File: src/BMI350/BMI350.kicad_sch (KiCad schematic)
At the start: 7 parts, among them U1 STM32H750VBTx, U2 BMM350

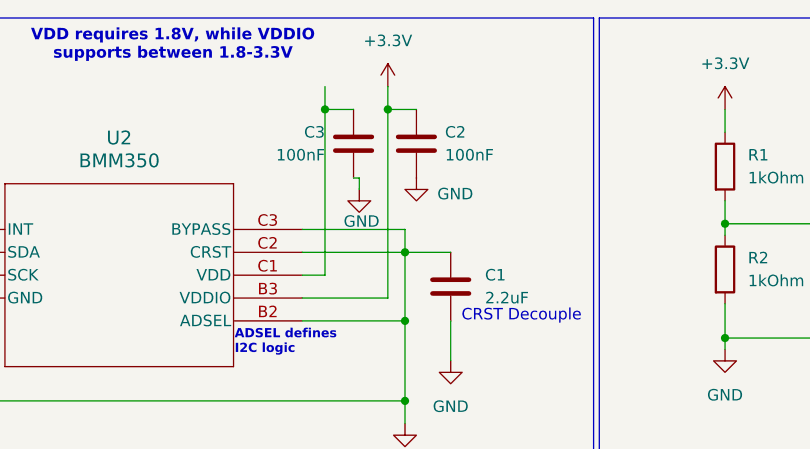
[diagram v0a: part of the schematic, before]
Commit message: BMM forgot
Forgot to save files before pushing
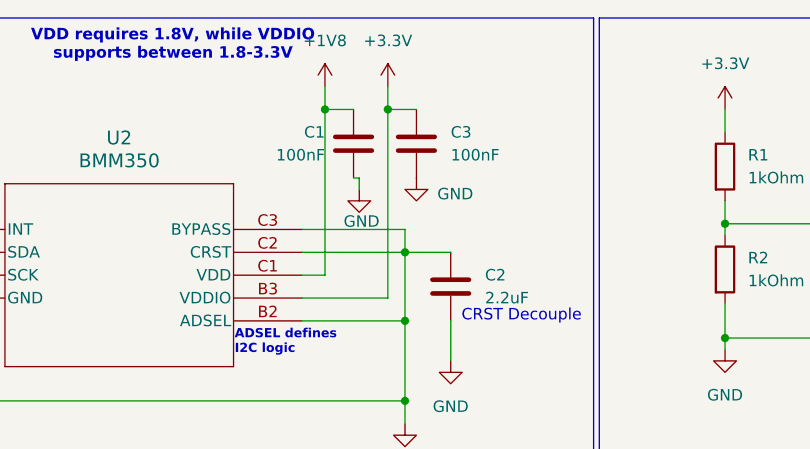
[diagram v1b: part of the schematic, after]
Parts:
- C1: renamed from C3; footprint Capacitor_SMD:C_0402_1005Metric -> Capacitor_SMD:C_0201_0603Metric
- C2: renamed from C1; footprint Capacitor_SMD:C_0402_1005Metric -> Capacitor_SMD:C_0201_0603Metric
- C3: renamed from C2; footprint Capacitor_SMD:C_0402_1005Metric -> Capacitor_SMD:C_0201_0603Metric
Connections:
- net +1V8: now also C1.2, U2.C1 (VDD)
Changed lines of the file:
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@@
 		(on_board yes)
 		(dnp no)
-		(property "Reference" "C3"
+		(property "Reference" "C1"
 			(at 156.21 26.6699 0)
 			(effects
@@
 			)
 		)
-		(property "Footprint" "Capacitor_SMD:C_0402_1005Metric"
+		(property "Footprint" "Capacitor_SMD:C_0201_0603Metric"
 			(at 160.3502 24.13 0)
 			(effects
@@
 			(project "BMI350"
 				(path "/5c9baf5e-0e0f-4389-833f-bb0eff9d07fc"
-					(reference "C3")
+					(reference "C1")
 					(unit 1)
 				)
@@
 	)
 	(symbol
+		(lib_id "power:+1V8")
+		(at 156.21 21.59 0)
+		(unit 1)
+		(exclude_from_sim no)
+		(in_bom yes)
+		(on_board yes)
+		(dnp no)
+		(fields_autoplaced yes)
+		(property "Reference" "#PWR03"
+			(at 156.21 25.4 0)
+			(effects
+				(font
+					(size 1.27 1.27)
+				)
+				(hide yes)
+			)
+		)
+		(property "Value" "+1V8"
+			(at 156.21 16.51 0)
+			(effects
+				(font
+					(size 1.27 1.27)
+				)
+			)
+		)
+		(property "Footprint" ""
+			(at 156.21 21.59 0)
+			(effects
+				(font
+					(size 1.27 1.27)
+				)
+				(hide yes)
+			)
+		)
+		(property "Datasheet" ""
+			(at 156.21 21.59 0)
+			(effects
+				(font
+					(size 1.27 1.27)
+				)
+				(hide yes)
+			)
+		)
+		(property "Description" "Power symbol creates a global label with name \"+1V8\""
+			(at 156.21 21.59 0)
+			(effects
+				(font
+					(size 1.27 1.27)
+				)
+				(hide yes)
+			)
+		)
+		(pin "1"
+		)
+		(instances
+			(project ""
+				(path "/5c9baf5e-0e0f-4389-833f-bb0eff9d07fc"
+					(reference "#PWR03")
+					(unit 1)
+				)
+			)
+		)
+	)
+	(symbol
 		(lib_id "Device:C")
 		(at 166.37 27.94 0)
@@
 		(dnp no)
 		(fields_autoplaced yes)
-		(property "Reference" "C2"
-			(at 169.545 26.6699 0)
+		(property "Reference" "C3"
+			(at 170.18 26.6699 0)
 			(effects
 				(font
@@
 		)
 		(property "Value" "100nF"
-			(at 169.545 29.2099 0)
+			(at 170.18 29.2099 0)
 			(effects
 				(font
@@
 			)
 		)
-		(property "Footprint" "Capacitor_SMD:C_0402_1005Metric"
+		(property "Footprint" "Capacitor_SMD:C_0201_0603Metric"
 			(at 167.3352 31.75 0)
 			(effects
@@
 			(project ""
 				(path "/5c9baf5e-0e0f-4389-833f-bb0eff9d07fc"
-					(reference "C2")
+					(reference "C3")
 					(unit 1)
 				)
@@
 		(dnp no)
 		(fields_autoplaced yes)
-		(property "Reference" "C1"
+		(property "Reference" "C2"
 			(at 173.99 42.5449 0)
 			(effects
@@
 			)
 		)
-		(property "Footprint" "Capacitor_SMD:C_0402_1005Metric"
+		(property "Footprint" "Capacitor_SMD:C_0201_0603Metric"
 			(at 171.1452 47.625 0)
 			(effects
@@
 			(project ""
 				(path "/5c9baf5e-0e0f-4389-833f-bb0eff9d07fc"
-					(reference "C1")
-					(unit 1)
-				)
+					(reference "C2")
+					(unit 1)
+				)

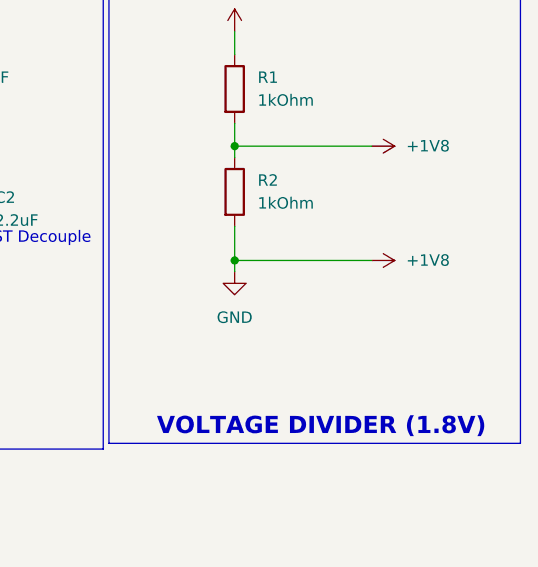
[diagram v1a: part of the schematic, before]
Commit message: Voltage Divider
Fixed voltage divider outputs
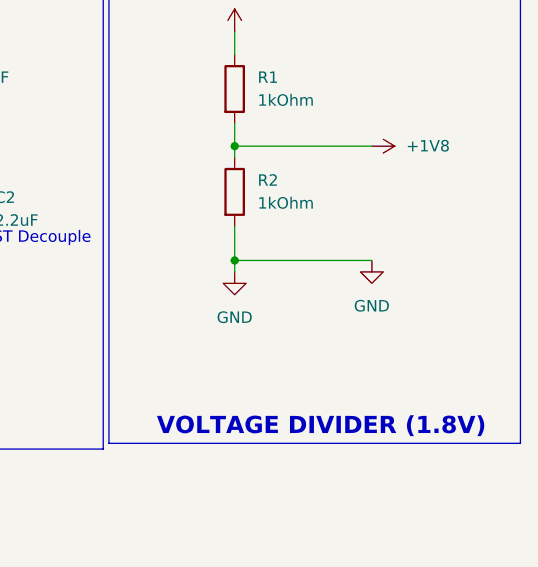
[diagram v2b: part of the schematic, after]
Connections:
- net +1V8: no longer C1.1, C2.1, C2.2, C3.2, R2.2, U2.B1 (GND), U2.B2 (ADSEL), U2.C2 (CRST), U2.C3 (BYPASS)
- new net GND: C1.1, C2.1, C2.2, C3.2, R2.2, U2.B1 (GND), U2.B2 (ADSEL), U2.C2 (CRST), U2.C3 (BYPASS)
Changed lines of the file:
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@@
-	)
-	(symbol
-		(lib_id "power:+1V8")
-		(at 215.9 49.53 270)
-		(unit 1)
-		(exclude_from_sim no)
-		(in_bom yes)
-		(on_board yes)
-		(dnp no)
-		(fields_autoplaced yes)
-		(property "Reference" "#PWR07"
-			(at 212.09 49.53 0)
-			(effects
-				(font
-					(size 1.27 1.27)
-				)
-				(hide yes)
-			)
-		)
-		(property "Value" "+1V8"
-			(at 219.71 49.5299 90)
-			(effects
-				(font
-					(size 1.27 1.27)
-				)
-				(justify left)
-			)
-		)
-		(property "Footprint" ""
-			(at 215.9 49.53 0)
-			(effects
-				(font
-					(size 1.27 1.27)
-				)
-				(hide yes)
-			)
-		)
-		(property "Datasheet" ""
-			(at 215.9 49.53 0)
-			(effects
-				(font
-					(size 1.27 1.27)
-				)
-				(hide yes)
-			)
-		)
-		(property "Description" "Power symbol creates a global label with name \"+1V8\""
-			(at 215.9 49.53 0)
-			(effects
-				(font
-					(size 1.27 1.27)
-				)
-				(hide yes)
-			)
-		)
-		(pin "1"
-		)
-		(instances
-			(project ""
-				(path "/5c9baf5e-0e0f-4389-833f-bb0eff9d07fc"
-					(reference "#PWR07")
-					(unit 1)
-				)
-			)
-		)
 	)
 	(symbol
@@
 					(unit 1)
 				)
+			)
+		)
+	)
+	(symbol
+		(lib_id "power:GND")
+		(at 215.9 49.53 0)
+		(unit 1)
+		(exclude_from_sim no)
+		(in_bom yes)
+		(on_board yes)
+		(dnp no)
+		(fields_autoplaced yes)
+		(property "Reference" "#PWR07"
+			(at 215.9 55.88 0)
+			(effects
+				(font
+					(size 1.27 1.27)
+				)
+				(hide yes)
+			)
+		)
+		(property "Value" "GND"
+			(at 215.9 54.61 0)
+			(effects
+				(font
+					(size 1.27 1.27)
+				)
+			)
+		)
+		(property "Footprint" ""
+			(at 215.9 49.53 0)
+			(effects
+				(font
+					(size 1.27 1.27)
+				)
+				(hide yes)
+			)
+		)
+		(property "Datasheet" ""
+			(at 215.9 49.53 0)
+			(effects
+				(font
+					(size 1.27 1.27)
+				)
+				(hide yes)
+			)
+		)
+		(property "Description" "Power symbol creates a global label with name \"GND\" , ground"
+			(at 215.9 49.53 0)
+			(effects
+				(font
+					(size 1.27 1.27)
+				)
+				(hide yes)
+			)
+		)
+		(pin "1"
+		)
+		(instances
+			(project ""
+				(path "/5c9baf5e-0e0f-4389-833f-bb0eff9d07fc"
+					(reference "#PWR07")
+					(unit 1)
+				)

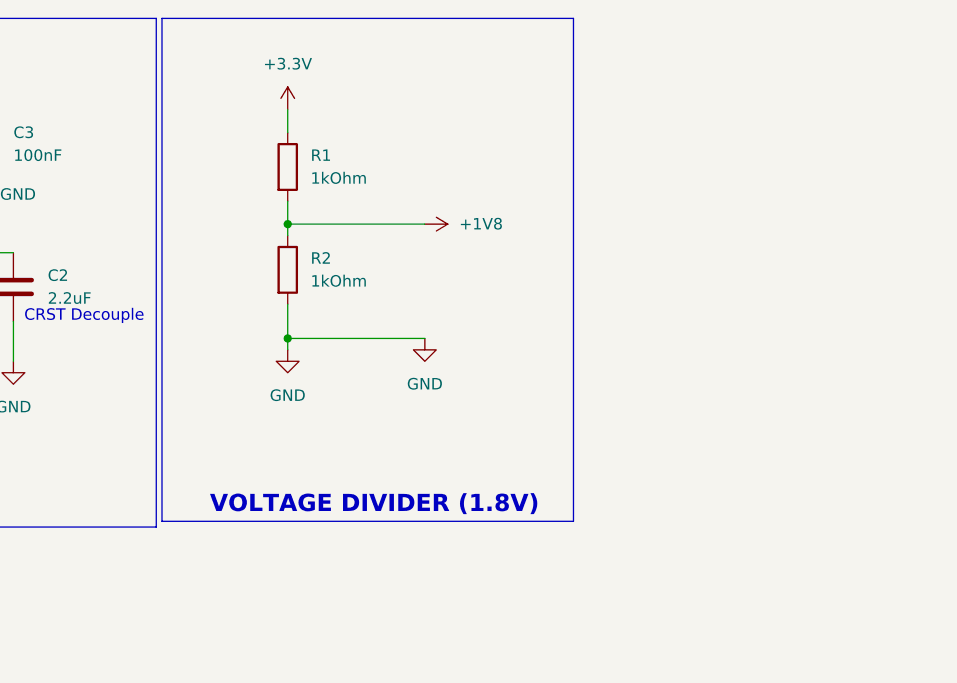
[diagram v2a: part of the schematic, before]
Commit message: Buck Converter
Redid BM350 breakout schematic with 3.3-1.8 buck converter instead of voltage divider
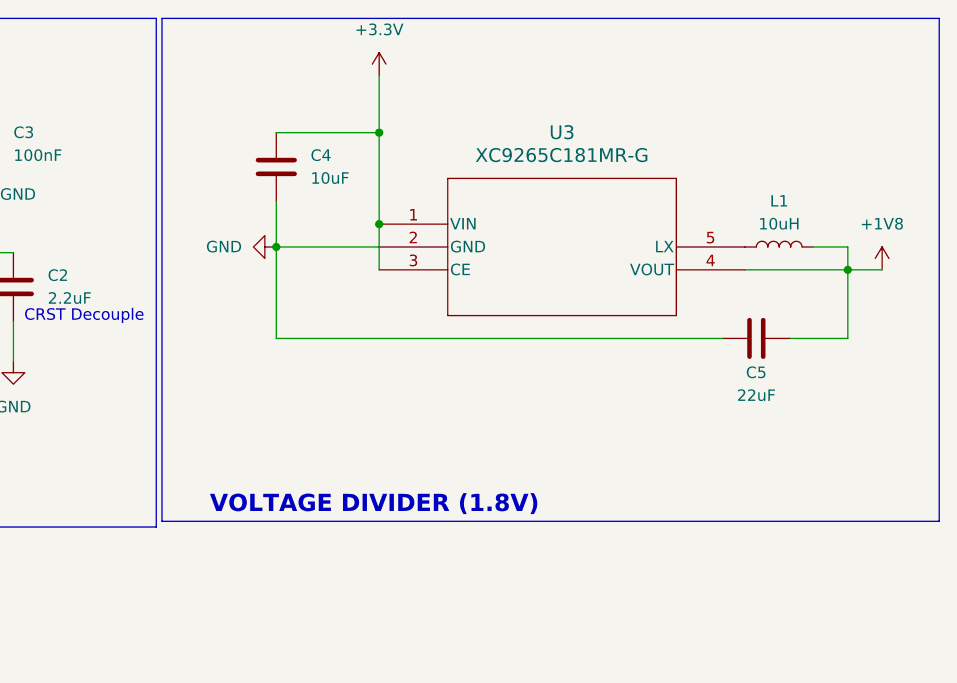
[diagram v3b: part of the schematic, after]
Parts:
- removed R1, R2: 1kOhm, Resistor_SMD:R_0201_0603Metric, symbol Device:R
- added C4: 10uF, Capacitor_SMD:C_0201_0603Metric, symbol Device:C
- added C5: 22uF, Capacitor_SMD:C_0201_0603Metric, symbol Device:C
- added L1: 10uH, Inductor_SMD:L_0201_0603Metric, symbol Device:L
- added U3: XC9265C181MR-G, XC9529:SOT_181MR-G_TOR, symbol XC9265:XC9265C181MR-G
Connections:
- net +1V8: now also C5.2, L1.2, U3.4 (VOUT)
- net +3.3V: now also C4.1, U3.1 (VIN), U3.3 (CE)
- net GND: now also C4.2, C5.1, U3.2 (GND)
- new net: L1.1, U3.5 (LX)

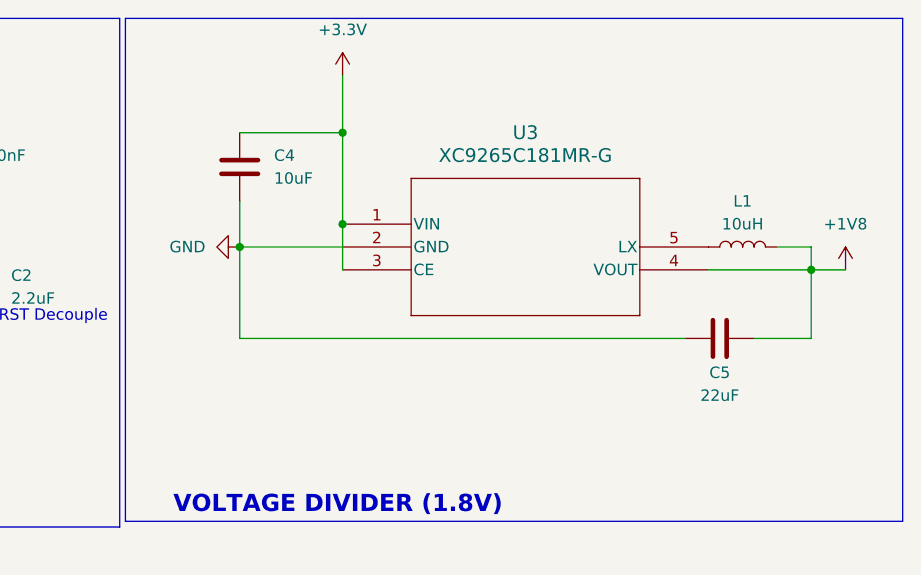
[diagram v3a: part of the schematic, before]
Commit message: S-85S1A
Added S-85S1A to flight computer schematic
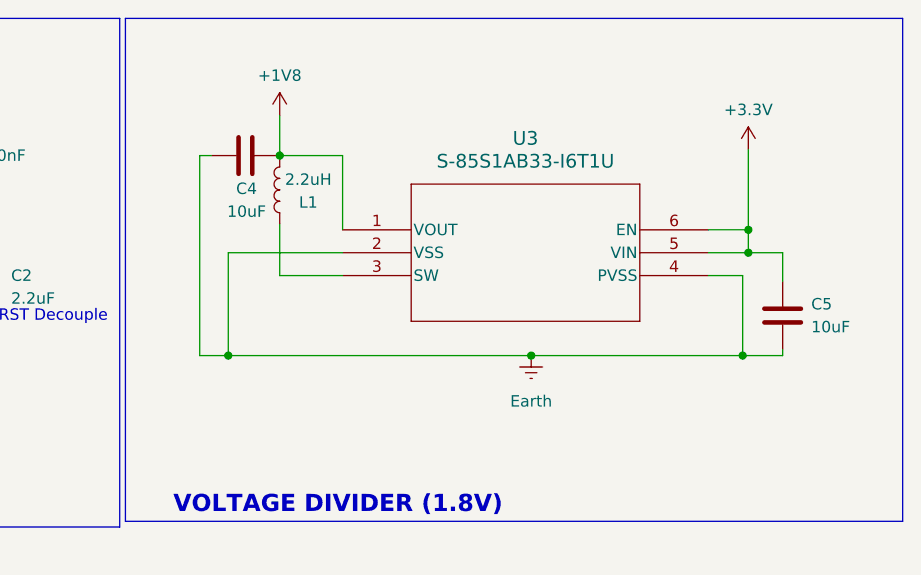
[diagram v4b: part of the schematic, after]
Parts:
- removed U3: XC9265C181MR-G, XC9529:SOT_181MR-G_TOR, symbol XC9265:XC9265C181MR-G
- added U3: S-85S1AB33-I6T1U, footprints:SNT-6A-A-PKG_PG006-A-P-SD-2.1_ABL, symbol S85S1:S-85S1AB33-I6T1U
- C5: value 22uF -> 10uF
- L1: value 10uH -> 2.2uH
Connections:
- net +1V8: now also C4.2, U3.1 (VOUT); no longer C5.2
- net +3.3V: now also C5.1, U3.5 (VIN), U3.6 (EN); no longer C4.1
- net GND: no longer C4.2, C5.1
- net at L1.1: now also U3.3 (SW)
- new net Earth: C4.1, C5.2, U3.2 (VSS), U3.4 (PVSS)

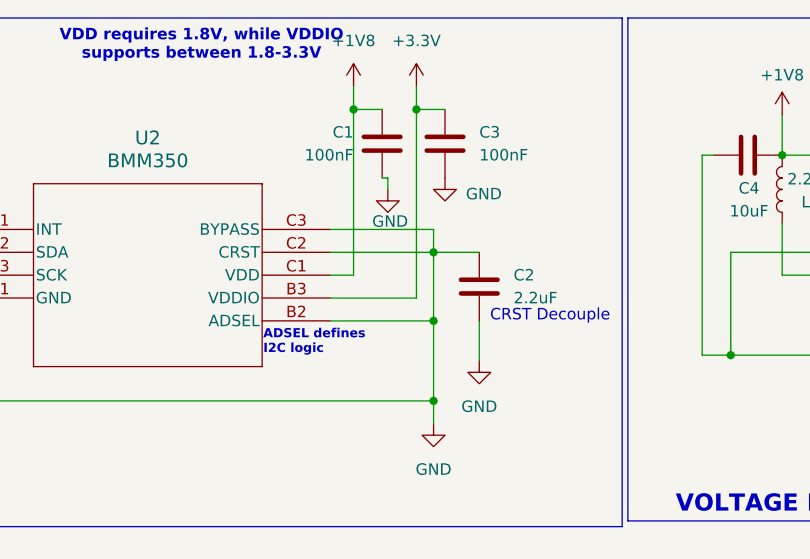
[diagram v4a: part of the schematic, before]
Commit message: quick fix
Fixed BMM350 decoupling capacitor issue
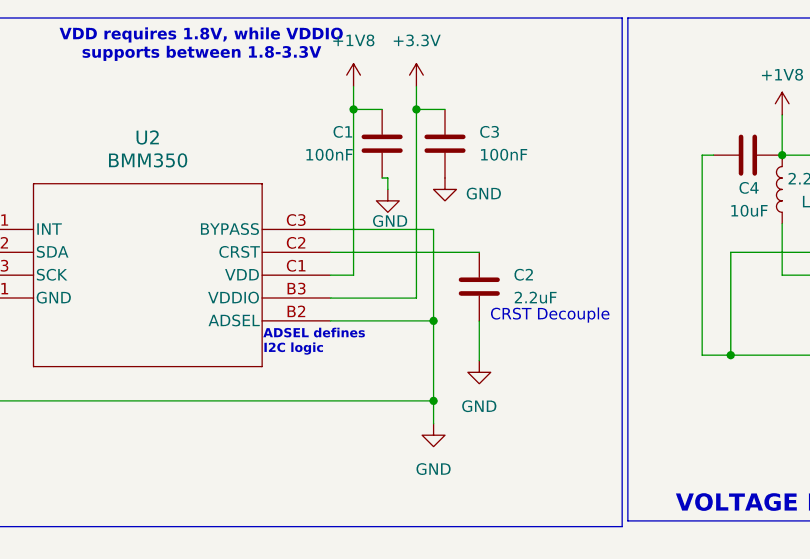
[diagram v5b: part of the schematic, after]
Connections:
- net GND: no longer C2.1, U2.C2 (CRST)
- new net: C2.1, U2.C2 (CRST)
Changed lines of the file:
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@@
-	)
-	(junction
-		(at 165.1 40.005)
-		(diameter 0)
-		(color 0 0 0 0)
 	)
 	(junction
@@
 	(wire
 		(pts
-			(xy 153.67 40.005) (xy 165.1 40.005)
-		)
-		(stroke
-			(width 0)
-			(type default)
-		)
-	)
-	(wire
-		(pts
 			(xy 109.22 37.465) (xy 113.03 37.465)
 		)
@@
 	(wire
 		(pts
-			(xy 165.1 37.465) (xy 165.1 40.005)
-		)
-		(stroke
-			(width 0)
-			(type default)
-		)
-	)
-	(wire
-		(pts
-			(xy 165.1 40.005) (xy 165.1 47.625)
+			(xy 165.1 37.465) (xy 165.1 47.625)
 		)
 		(stroke
@@
 	(wire
 		(pts
-			(xy 165.1 40.005) (xy 170.18 40.005)
-		)
-		(stroke
+			(xy 153.67 40.005) (xy 170.18 40.005)
+		)
+		(stroke
